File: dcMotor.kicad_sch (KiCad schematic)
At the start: 112 parts, among them J1 Conn_01x06_Pin, J2 Conn_01x02_Pin, J3 USB_C_Receptacle_USB2.0_16P, J4 Conn_Staubli_SLB4-F6,3-rot, J5 Conn_Staubli_SLB4-F6,3, J6 Conn_ST_STDC14, J7 USB_C_Receptacle_USB2.0_16P, J8 Conn_01x04_Pin, Q2 AO3400A, SW3 SW_Push, SW4 SW_Push, U1 NCP718xSN500, U10 TLV9152IDR, U3 NCP718ASNADJT1G, U4 DRV8231ADDA, U5 MCP6561-OT, U6 STM32G431CBTx, U7 ER_OLEDM0.91_1x-I2C, U8 LMR54406DBVR, U9 LTH-301-05

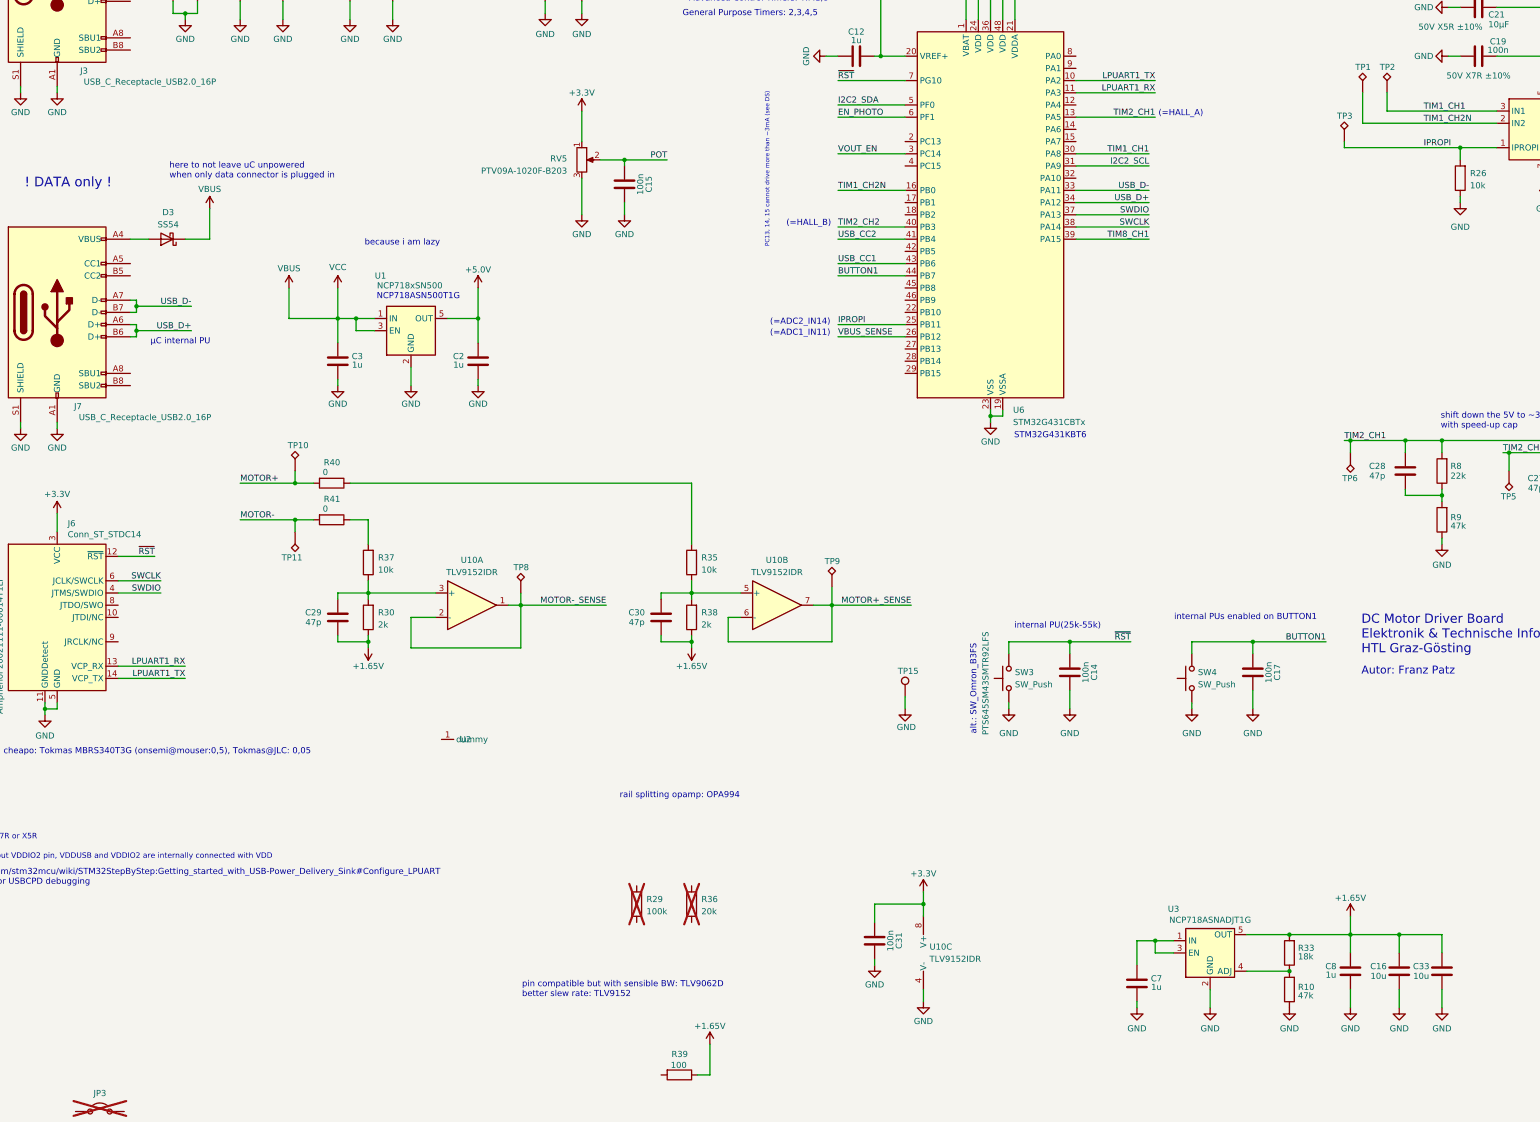
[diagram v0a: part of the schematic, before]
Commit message: design blocks for linear regulators
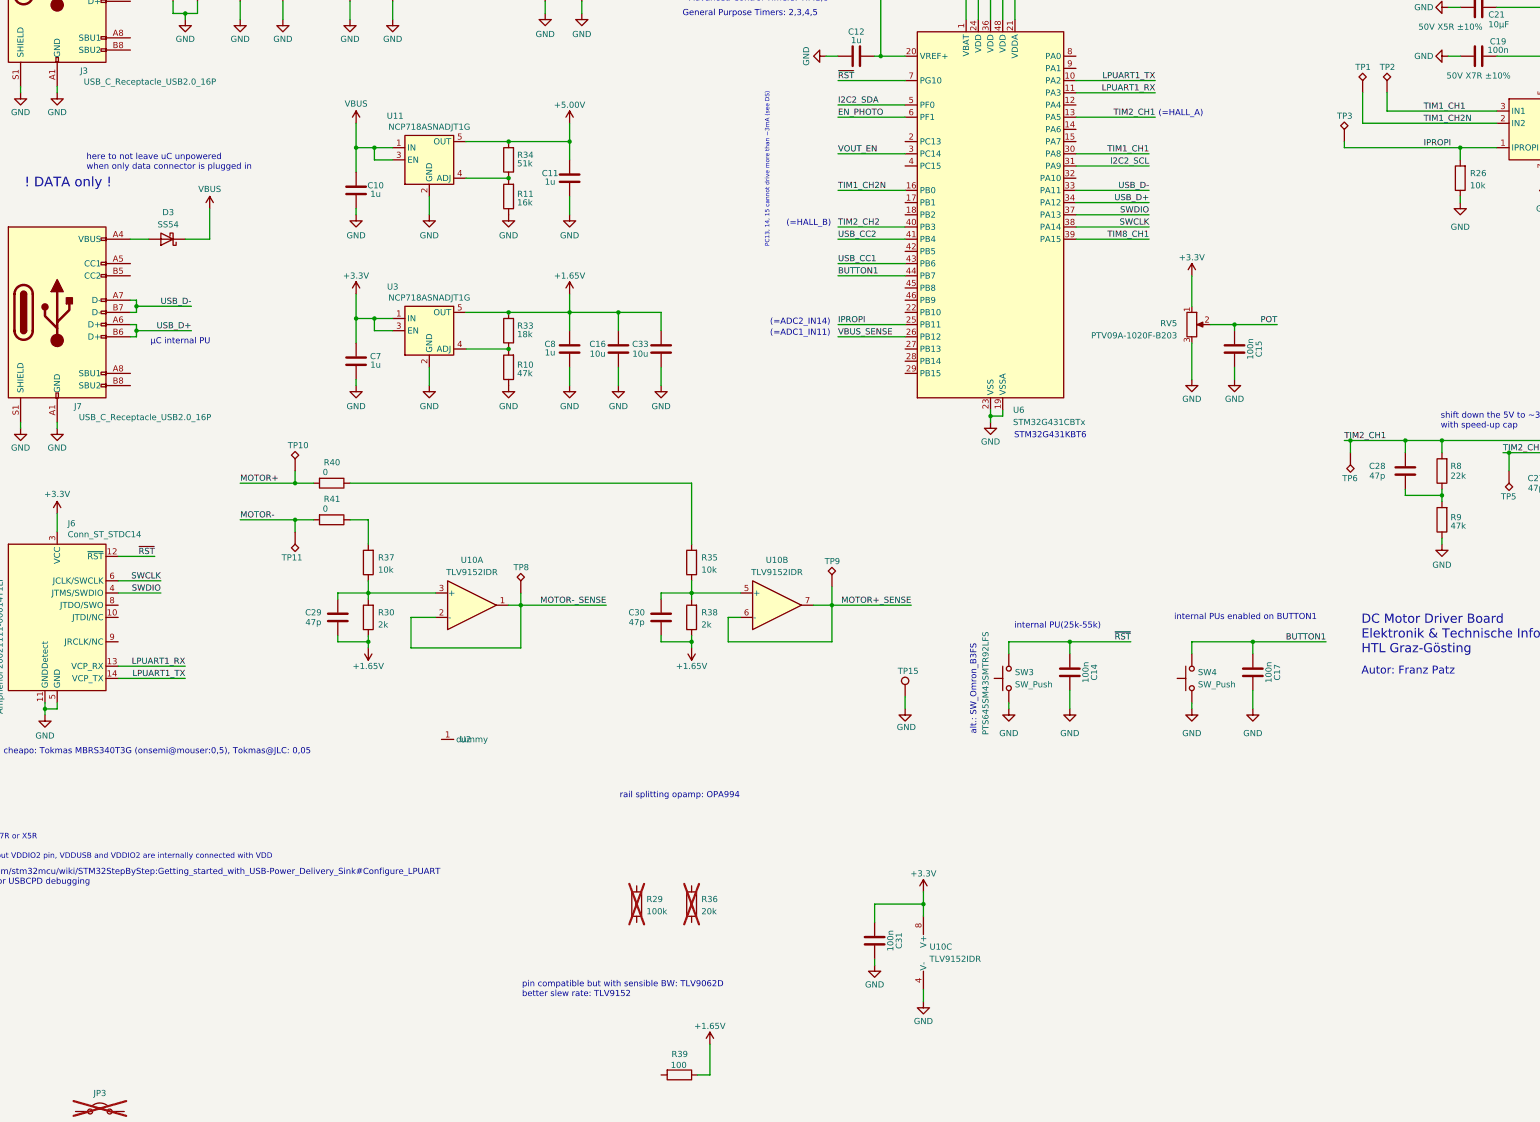
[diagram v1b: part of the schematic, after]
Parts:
- removed C2, C3: 1u, Capacitor_SMD:C_0805_2012Metric_Pad1.18x1.45mm_HandSolder, symbol Device:C
- removed U1: NCP718xSN500, Package_TO_SOT_SMD:SOT-23-5, symbol Regulator_Linear:NCP718xSN500
- added C10, C11: 1u, Capacitor_SMD:C_0805_2012Metric_Pad1.18x1.45mm_HandSolder, symbol Device:C
- added R11: 16k, Resistor_SMD:R_0805_2012Metric_Pad1.20x1.40mm_HandSolder, symbol Device:R
- added R34: 51k, Resistor_SMD:R_0805_2012Metric, symbol Device:R
- added U11: NCP718ASNADJT1G, Package_TO_SOT_SMD:SOT-23-5, symbol PZ:NCP718ASNADJT1G
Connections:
- net +3.3V: now also C7.2, U3.1 (IN), U3.3 (EN)
- net GND: now also C10.1, C11.1, R11.1, U11.2 (GND)
- net VBUS: now also C10.2, U11.1 (IN), U11.3 (EN)
- net at U3.4 (ADJ): now also R10.2, R33.1
- new net: R11.2, R34.1, U11.4 (ADJ)
- new net +5.00V: C11.2, R34.2, U11.5 (OUT)
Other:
- note removed: "NCP718ASN500T1G"
- note removed: "because i am lazy"
- moved on the sheet: C15, C16, C33, C7, C8, R10, R33, RV5, U3

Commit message: backup commit before reannotation
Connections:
- net MOTOR+_SENSE: now also U6.8 (PA0)
- net MOTOR-_SENSE: now also U6.9 (PA1)
- net at U3.4 (ADJ): now also R10.2, R33.1
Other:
- note added: "(=ADC2_IN1)"
- note added: "(=ADC2_IN2)"
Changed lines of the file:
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@@
 		)
 	)
+	(text "(=ADC2_IN1)"
+		(exclude_from_sim no)
+		(at 265.176 137.668 0)
+		(effects
+			(font
+				(size 1.27 1.27)
+			)
+		)
+	)
 	(text "internal PU(25k-55k)"
 		(exclude_from_sim no)
@@
 		)
 	)
+	(text "(=ADC2_IN2)"
+		(exclude_from_sim no)
+		(at 265.176 140.208 0)
+		(effects
+			(font
+				(size 1.27 1.27)
+			)
+		)
+	)
 	(text "(=HALL_A)"
 		(exclude_from_sim no)
@@
 	(wire
 		(pts
+			(xy 242.57 138.43) (xy 257.81 138.43)
+		)
+		(stroke
+			(width 0)
+			(type default)
+		)
+	)
+	(wire
+		(pts
 			(xy 191.77 252.73) (xy 187.96 252.73)
 		)
@@
 	(wire
 		(pts
+			(xy 242.57 140.97) (xy 257.81 140.97)
+		)
+		(stroke
+			(width 0)
+			(type default)
+		)
+	)
+	(wire
+		(pts
 			(xy 27.94 273.05) (xy 27.94 274.32)
 		)
@@
 		)
 	)
+	(label "MOTOR+_SENSE"
+		(at 257.81 138.43 180)
+		(effects
+			(font
+				(size 1.27 1.27)
+			)
+			(justify right bottom)
+		)
+	)
 	(label "~{RST}"
 		(at 193.04 143.51 0)
@@
 		)
 	)
+	(label "MOTOR-_SENSE"
+		(at 257.81 140.97 180)
+		(effects
+			(font
+				(size 1.27 1.27)
+			)
+			(justify right bottom)
+		)
+	)

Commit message: reannotated
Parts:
- renumbered C24 to C1, C26 to C10, C8 to C12, C16 to C13, C33 to C14, C30 to C15, C23 to C16, C12 to C17, C31 to C18, C41 to C19, C4 to C2, C42 to C20, C43 to C21, C44 to C22, C45 to C23, C14 to C24, C15 to C25, C17 to C26, C28 to C27, C18 to C28, C22 to C29, C9 to C3, C21 to C30, C19 to C31, C27 to C32, C25 to C33, C20 to C34, C32 to C35, C5 to C4, C6 to C5, C29 to C6, C13 to C7, C10 to C8, C7 to C9, D5 to D1, D3 to D2, D2 to D3, D7 to D5, D1 to D6, D6 to D7, FB4 to FB1, J3 to J1, J7 to J2, J6 to J3, J5 to J4, J4 to J5, J2 to J6, J8 to J7, J1 to J8, JP3 to JP1, L2 to L1, L1 to L2, Q2 to Q1, R34 to R10, R33 to R12, R10 to R13, R2 to R14, R3 to R15, R29 to R16, R21 to R17, R39 to R18, R20 to R19, R4 to R2, R35 to R20, R38 to R21, R36 to R22, R22 to R23, R27 to R24, R8 to R25, R9 to R26, R26 to R27, R31 to R29, R40 to R3, R6 to R30, R7 to R31, R41 to R4, R23 to R5, R37 to R6, R30 to R7, R24 to R8, R5 to R9, RV5 to RV1, SW3 to SW1, SW4 to SW2, TP10 to TP1, TP2 to TP10, TP5 to TP11, TP7 to TP12, TP11 to TP2, TP8 to TP3, TP9 to TP4, TP15 to TP5, TP3 to TP6, TP6 to TP7, TP1 to TP8, TP4 to TP9, U8 to U1, U5 to U10, U11 to U2, U2 to U4, U10 to U5, U7 to U6, U6 to U7, U9 to U8, U4 to U9
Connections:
- net at U3.4 (ADJ): now also R12.1, R13.2

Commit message: wip
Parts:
- removed J4: Conn_Staubli_SLB4-F6,3, PZ:Staubli_SLB4-F6,3-schwarz, symbol PZ:Conn_Staubli_SLB4-F6,3-schwarz
- removed J5: Conn_Staubli_SLB4-F6,3-rot, PZ:Staubli_SLB4-F6,3-rot, symbol PZ:Conn_Staubli_SLB4-F6,3-rot
- removed R18: 100, Resistor_SMD:R_0805_2012Metric, symbol Device:R
- added C36: 100µ, Capacitor_SMD:CP_Elec_6.3x7.7, symbol Device:C_Polarized
- added TP13, TP14: TestPoint_Keystone_5019, PZ:TestPoint_Keystone_5019_Miniature, symbol PZ:TestPoint_Keystone_5019
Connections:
- net +5.00V is gone; now on net +5.0V: C11.2, R10.2, U2.5 (OUT)
- net TIM8_CH1 is gone; now on net BUTTON1: U7.39 (PA15)
- net BUTTON1: no longer U7.44 (PB7)
- net EN_PHOTO: now also U7.12 (PA4); no longer U7.6 (PF1)
- net GND: now also C36.2, TP13.1, TP14.1
- net POT: now also U7.28 (PB14)
- net VBUS: now also C36.1
- net at U3.4 (ADJ): now also R12.1, R13.2
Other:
- note added: "(=ADC1_IN5)"
- note added: "pin compatible with MCP6002 TLV9062D"
- note removed: "All ceramic caps X7R or X5R"
- note removed: "Notes"
- note removed: "On packages without VDDIO2 pin, VDDUSB and VDDIO2 are internally connected with VDD"
- note removed: "https://wiki.st.com/stm32mcu/wiki/STM32StepByStep:Getting_started_with_USB-Power_Delivery_Sink#Configure_LPUART 921600 bauds for USBCPD debugging"
- note removed: "pin compatible but with sensible BW: TLV9062D better slew rate: TLV9152"
- moved on the sheet: C18, C24, C25, C27, C28, C29, C30, C31, C32, C33, C34, D7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

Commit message: finished prel routing
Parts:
- added C37: 10µF, Capacitor_SMD:C_0805_2012Metric_Pad1.18x1.45mm_HandSolder, symbol Device:C
- added C38: 10u, Capacitor_SMD:C_0805_2012Metric, symbol Device:C
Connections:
- net +3.3V: now also C38.2
- net GND: now also C37.2, C38.1
- net VBUS: now also C37.1
- net at U3.4 (ADJ): now also R12.1, R13.2
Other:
- note added: "long distance"
- moved on the sheet: C18, C28, C35, C36, R28, R29, R32, TP12, U10, U5C

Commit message: prel design done
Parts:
- added TP15, TP16: TestPoint_Keystone_5019, PZ:TestPoint_Keystone_5019_Miniature, symbol PZ:TestPoint_Keystone_5019
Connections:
- net GND: now also TP15.1, TP16.1
- net at U3.4 (ADJ): now also R12.1, R13.2

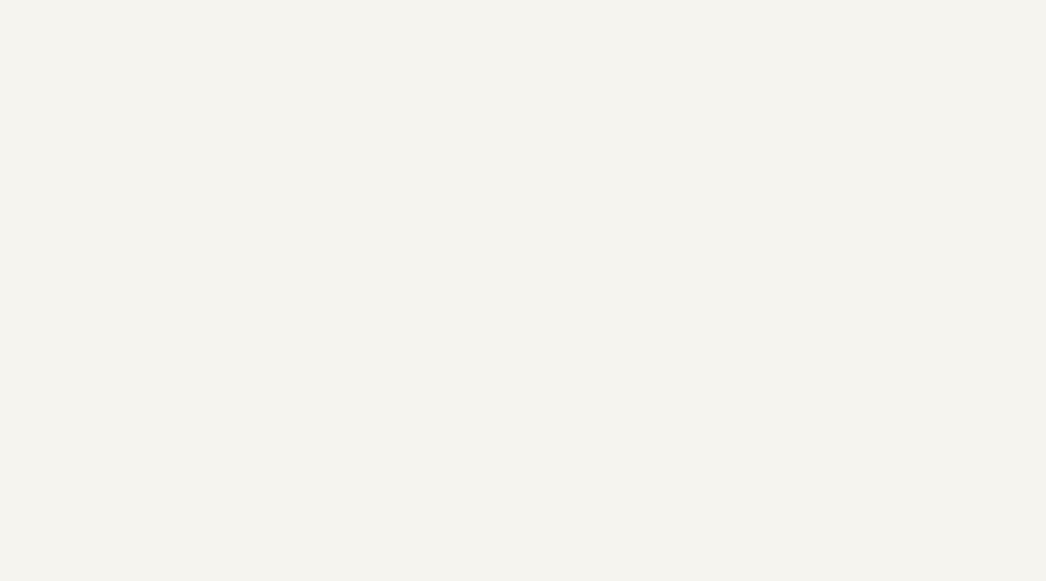
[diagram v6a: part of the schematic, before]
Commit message: added nucleo fpr MATLAB, still cutouts are missing
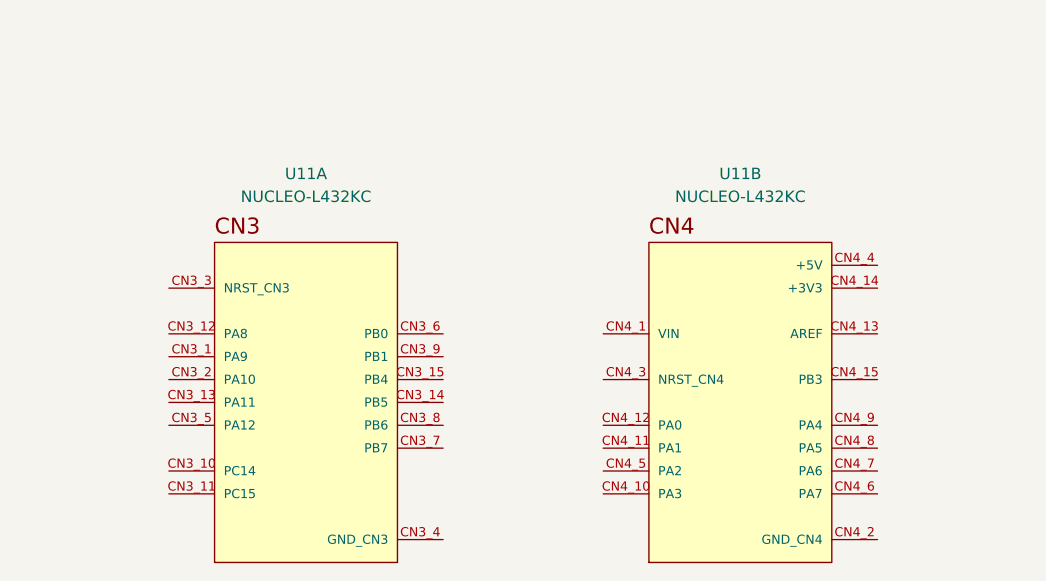
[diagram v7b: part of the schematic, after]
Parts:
- added U11: NUCLEO-L432KC, local:MODULE_NUCLEO-L432KC, symbol NUCLEO-L432KC:NUCLEO-L432KC
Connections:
- net at U3.4 (ADJ): now also R12.1, R13.2

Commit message: wip
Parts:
- U11: now not fitted; now left out of the parts list
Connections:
- net at U3.4 (ADJ): now also R12.1, R13.2
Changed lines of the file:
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@@
 		(body_style 1)
 		(exclude_from_sim no)
-		(in_bom yes)
-		(on_board yes)
-		(in_pos_files yes)
-		(dnp no)
+		(in_bom no)
+		(on_board no)
+		(in_pos_files no)
+		(dnp yes)
 		(fields_autoplaced yes)
 		(property "Reference" "U11"
@@
 		)
 		(property "LCSC Part #" ""
+			(at 213.36 328.93 0)
+			(hide yes)
+			(show_name no)
+			(do_not_autoplace no)
+			(effects
+				(font
+					(size 1.27 1.27)
+				)
+			)
+		)
+		(property "FT Rotation Offset" ""
 			(at 213.36 328.93 0)
 			(hide yes)
@@
 		(body_style 1)
 		(exclude_from_sim no)
-		(in_bom yes)
-		(on_board yes)
-		(in_pos_files yes)
-		(dnp no)
+		(in_bom no)
+		(on_board no)
+		(in_pos_files no)
+		(dnp yes)
 		(fields_autoplaced yes)
 		(property "Reference" "U11"
@@
 			(at 261.62 328.93 0)
 			(hide yes)
+			(show_name no)
+			(do_not_autoplace no)
+			(effects
+				(font
+					(size 1.27 1.27)
+				)
+			)
+		)
+		(property "FT Rotation Offset" ""
+			(at 261.62 328.93 0)
+			(hide yes)
